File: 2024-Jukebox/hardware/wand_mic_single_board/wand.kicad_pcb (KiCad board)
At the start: 4 copper layers, 17.5 x 39 mm, 50 parts, among them J1 USB_C_Receptacle_USB2.0, J10 Conn_01x03, J4 Conn_01x02, J6 Conn_01x01, J9 Conn_01x02, Q1 MUN5214DW1T1G, Q3 CJ3139K, U1 CP2104, U2 ESP32-PICO-D4, U3 ICM-20948, U4 TP4065-4.2V, U5 TLV76718DRVx, U6 LY68L6400SLIT, U7 PCA9306, U9 TLV76733DRVx

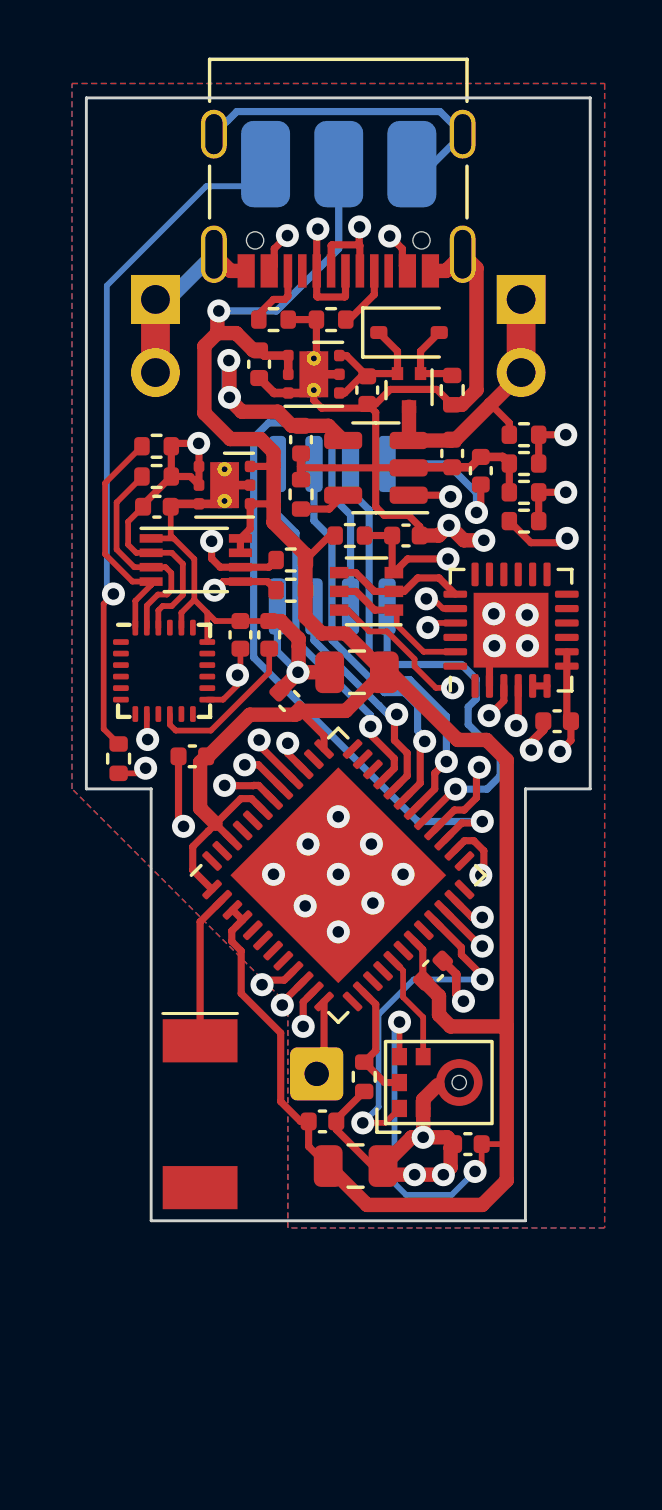
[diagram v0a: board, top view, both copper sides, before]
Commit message: Added some extra silkscreen indicators
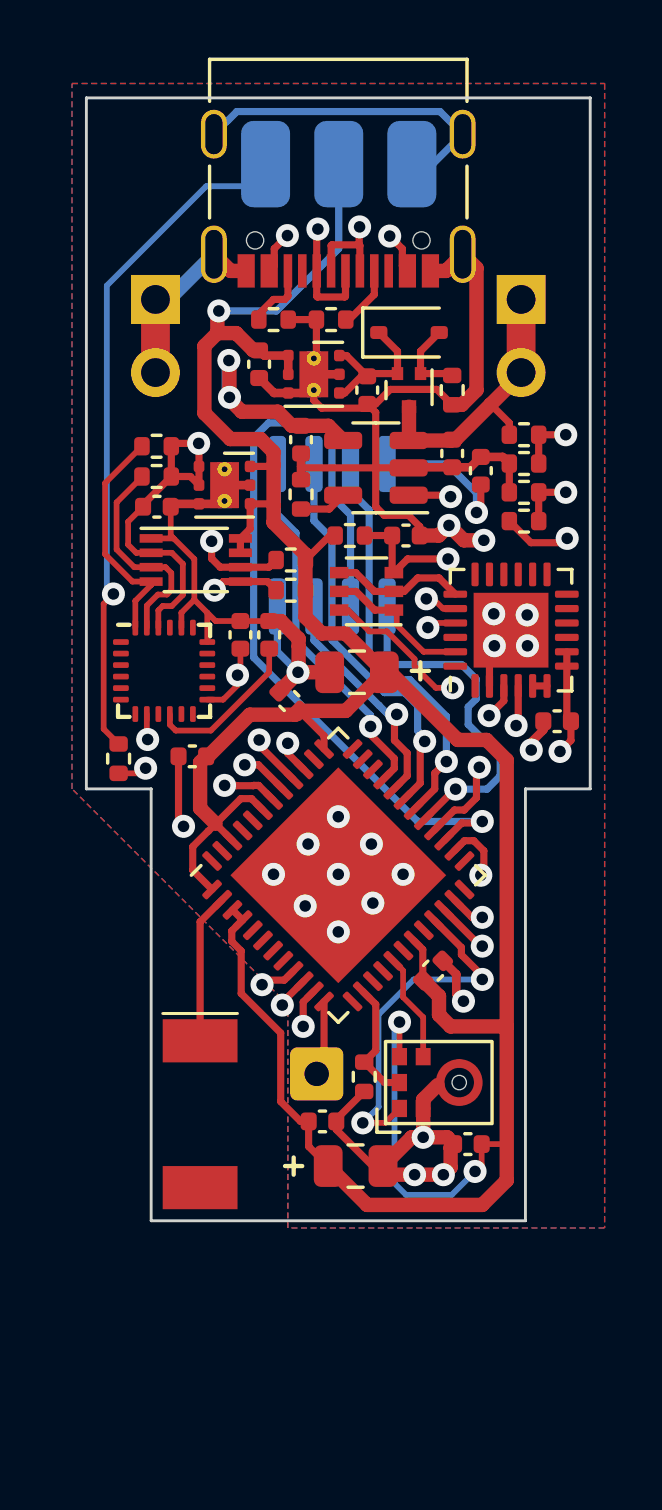
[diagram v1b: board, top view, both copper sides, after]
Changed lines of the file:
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@@
   (gr_line (start 12.95 32.8) (end 12.95 34.2)
     (stroke (width 0.15) (type default)) (layer "B.SilkS"))
+  (gr_line (start 7.2 36.8) (end 7.2 37.4)
+    (stroke (width 0.15) (type default)) (layer "F.SilkS"))
+  (gr_line (start 11.3 19.9) (end 11.9 19.9)
+    (stroke (width 0.15) (type default)) (layer "F.SilkS"))
+  (gr_line (start 11.6 19.6) (end 11.6 20.2)
+    (stroke (width 0.15) (type default)) (layer "F.SilkS"))
+  (gr_line (start 6.9 37.1) (end 7.5 37.1)
+    (stroke (width 0.15) (type default)) (layer "F.SilkS"))
   (gr_line (start 17.5 0) (end 17.5 24)
     (stroke (width 0.1) (type default)) (layer "Edge.Cuts"))
@@
   (segment (start 8.255025 31.384062) (end 8.255025 33.644975) (width 0.25) (layer "F.Cu") (net 92))
   (segment (start 8.255025 33.644975) (end 8 33.9) (width 0.25) (layer "F.Cu") (net 92))
+  (zone (net 0) (net_name "") (layers "F.Cu" "In1.Cu" "In2.Cu" "B.Cu") (hatch edge 0.5)
+    (connect_pads (clearance 0))
+    (min_thickness 0.25) (filled_areas_thickness no)
+    (keepout (tracks not_allowed) (vias not_allowed) (pads not_allowed) (copperpour not_allowed) (footprints allowed))
+    (fill (thermal_gap 0.5) (thermal_bridge_width 0.5))
+    (polygon
+      (pts
+        (xy 1.6 18.8)
+        (xy 1.6 21)
+        (xy 3.8 21)
+        (xy 3.8 18.8)
+      )
+    )
+  )
   (zone (net 6) (net_name "GND") (layers "F.Cu" "In1.Cu" "In2.Cu" "B.Cu") (hatch edge 0.5)
     (connect_pads (clearance 0.508))

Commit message: Updated wand PCBs
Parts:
- removed C14, C15: 47u, Capacitor_SMD:C_0805_2012Metric
- added C22: 10u, Capacitor_SMD:C_0402_1005Metric, F.Cu at (3.34, 30.4)
- added C23: 10u, Capacitor_SMD:C_0402_1005Metric, F.Cu at (3.35, 41.5)
- added C24: 10u, Capacitor_SMD:C_0402_1005Metric, F.Cu at (14.2, 32.9)
- added C25: 10u, Capacitor_SMD:C_0402_1005Metric, F.Cu at (12.5, 42.2)
- C9: footprint Capacitor_SMD:C_0402_1005Metric -> Capacitor_SMD:C_0603_1608Metric
- moved J10 28.3 mm to (13.5, 29.7), turned to 0 degrees
- moved C16 22.5 mm to (11.8, 43.0), turned to -45 degrees
- moved C5 20.2 mm to (7.70, 32.2), turned to 45 degrees
- moved C11 17.3 mm to (13.2, 24.9), turned to 0 degrees
- moved U9 14.6 mm to (13.5, 23.1), turned to 90 degrees
- moved C3 14.2 mm to (11.9, 8.15), turned to 90 degrees
- moved R11 14.1 mm to (11.4, 32.6), turned to -135 degrees
- moved J6 13.1 mm to (13.8, 45.6)
- moved C10 12.0 mm to (15.1, 20.9), turned to 180 degrees
- moved D1 11.7 mm to (14.3, 19.4), turned to 180 degrees
- moved R18 10.8 mm to (13.1, 20.9), turned to 180 degrees
- moved U2 10.8 mm to (8.75, 37.8), turned to 135 degrees
- moved AE1 10.2 mm to (5.95, 45.4), turned to 180 degrees
- moved U5 10.1 mm to (10.8, 21.6), turned to -90 degrees
- moved U1 9.99 mm to (8.75, 10.5), turned to 180 degrees
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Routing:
- net GND: track 94.0 -> 146.8 mm
- net VBUS: track 49.5 -> 23.9 mm, vias 6 -> 0
- net RXD: track 11.7 -> 33.3 mm
- net GPIO10: track 12.4 -> 33.8 mm
- net TXD: track 14.3 -> 35.0 mm
- net Net-(J10-Pin_1): track 23.6 -> 4.51 mm
- net GPIO2: track 19.7 -> 1.56 mm, vias 2 -> 0
- net GPIO25: track 4.33 -> 21.6 mm, vias 0 -> 2
- net GPIO0: track 15.5 -> 32.6 mm
- net GPIO7: track 8.15 -> 23.5 mm
- net IMU_SCL: track 12.3 -> 27.6 mm
- net RESET: track 24.0 -> 39.2 mm
- net GPIO9: track 17.5 -> 32.2 mm
- net Net-(U1-D+): track 27.1 -> 12.6 mm
- net IMU_SDA: track 12.4 -> 26.3 mm
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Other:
- board size 17.5 x 39 mm -> 17.5 x 47 mm
- board text added: "SRAM"

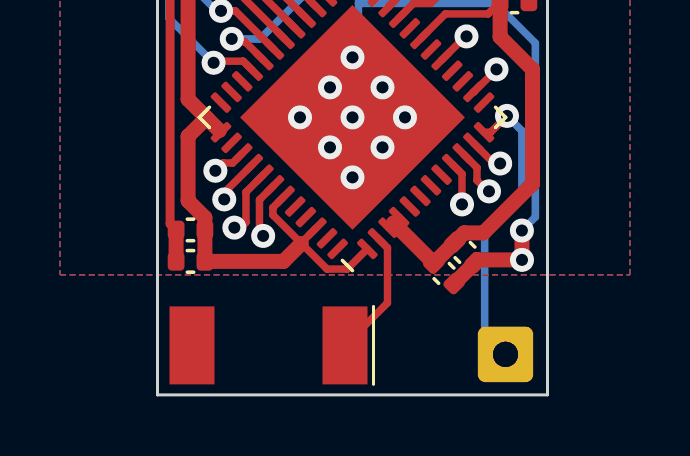
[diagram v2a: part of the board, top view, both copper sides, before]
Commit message: Added 3D models
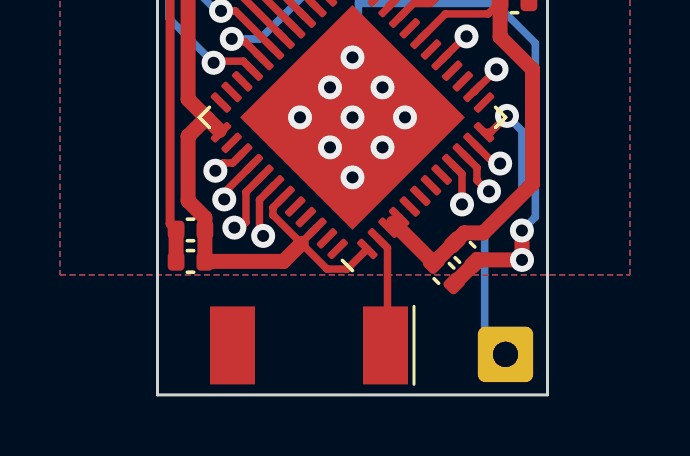
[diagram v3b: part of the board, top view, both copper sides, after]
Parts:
- moved AE1 1.35 mm to (7.30, 45.4)
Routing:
- net Net-(AE1-FEED): track 4.29 -> 3.73 mm
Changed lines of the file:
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@@
   (net 92 "Net-(J6-Pin_1)")
   (footprint "AlexCustom:NN01-102" (layer "F.Cu")
-    (at 5.95 45.35 180)
+    (at 7.3 45.35 180)
     (property "Sheetfile" "wand.kicad_sch")
     (property "Sheetname" "")
@@
     (pad "2" smd rect (at 2.55 0 180) (size 1.5 2.6) (layers "F.Cu" "F.Paste" "F.Mask")
       (net 90 "unconnected-(AE1-PCB_Trace-Pad2)") (pinfunction "PCB_Trace") (pintype "passive") (thermal_bridge_angle 45))
+    (model "${KIPRJMOD}/cad/NN01-102--3DModel-STEP-56544.STEP"
+      (offset (xyz 0 0 0))
+      (scale (xyz 1 1 1))
+      (rotate (xyz -90 0 0))
+    )
   )
   (footprint "Resistor_SMD:R_0402_1005Metric" (layer "F.Cu")
@@
     (pad "2" thru_hole oval (at 0 -2.54 180) (size 1.7 1.7) (drill 1) (layers "*.Cu" "*.Mask")
       (net 6 "GND") (pinfunction "Pin_2") (pintype "passive"))
-    (model "${KICAD6_3DMODEL_DIR}/Connector_PinHeader_2.54mm.3dshapes/PinHeader_1x02_P2.54mm_Vertical.wrl"
-      (offset (xyz 0 0 0))
-      (scale (xyz 1 1 1))
-      (rotate (xyz 0 0 0))
-    )
   )
   (footprint "Connector_PinHeader_2.54mm:PinHeader_1x03_P2.54mm_Vertical" (layer "B.Cu")
@@
     (pad "2" thru_hole oval (at 0 -2.54 180) (size 1.7 1.7) (drill 1) (layers "*.Cu" "*.Mask")
       (net 65 "+BATT") (pinfunction "Pin_2") (pintype "passive"))
-    (model "${KICAD6_3DMODEL_DIR}/Connector_PinHeader_2.54mm.3dshapes/PinHeader_1x02_P2.54mm_Vertical.wrl"
-      (offset (xyz 0 0 0))
+    (model "${KIPRJMOD}/cad/wand_battery_switch.step"
+      (offset (xyz -3.75 8 2))
       (scale (xyz 1 1 1))
       (rotate (xyz 0 0 0))
@@
   (segment (start 10.5125 19) (end 11.23 19.7175) (width 0.2) (layer "F.Cu") (net 78))
   (segment (start 9.598528 41.780509) (end 9.916542 42.098523) (width 0.25) (layer "F.Cu") (net 79))
-  (segment (start 9.916542 43.933458) (end 8.5 45.35) (width 0.25) (layer "F.Cu") (net 79))
-  (segment (start 9.916542 42.098523) (end 9.916542 43.933458) (width 0.25) (layer "F.Cu") (net 79))
+  (segment (start 9.916542 45.283458) (end 9.85 45.35) (width 0.25) (layer "F.Cu") (net 79))
+  (segment (start 9.916542 42.098523) (end 9.916542 45.283458) (width 0.25) (layer "F.Cu") (net 79))
   (segment (start 13.264986 40.214986) (end 12.899873 39.849873) (width 0.25) (layer "F.Cu") (net 80))
   (segment (start 14.28 17.73) (end 14.35 17.8) (width 0.25) (layer "F.Cu") (net 80))

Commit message: Updated wand PCB
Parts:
- moved AE1 1.40 mm to (5.90, 45.4)
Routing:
- net Net-(AE1-FEED): track 3.73 -> 4.31 mm
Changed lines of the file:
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@@
   (net 92 "Net-(J6-Pin_1)")
   (footprint "AlexCustom:NN01-102" (layer "F.Cu")
-    (at 7.3 45.35 180)
+    (at 5.9 45.35 180)
     (property "Sheetfile" "wand.kicad_sch")
     (property "Sheetname" "")
@@
         (effects (font (size 1 1) (thickness 0.15)) (justify mirror))
     )
-    (fp_text value "Conn_01x02" (at -20.25 -5.07) (layer "B.Fab")
+    (fp_text value "Conn_01x02" (at 2.37 -1.6 90) (layer "B.Fab")
         (effects (font (size 1 1) (thickness 0.15)) (justify mirror))
     )
@@
         (effects (font (size 1 1) (thickness 0.15)) (justify mirror))
     )
-    (fp_text value "Conn_01x02" (at -20.25 -5.07) (layer "B.Fab")
+    (fp_text value "Conn_01x02" (at -2.17 -1.2 90) (layer "B.Fab")
         (effects (font (size 1 1) (thickness 0.15)) (justify mirror))
     )
@@
       (net 65 "+BATT") (pinfunction "Pin_2") (pintype "passive"))
     (model "${KIPRJMOD}/cad/wand_battery_switch.step"
-      (offset (xyz -3.75 8 2))
+      (offset (xyz -3.75 8 2.5))
       (scale (xyz 1 1 1))
       (rotate (xyz 0 0 0))
@@
   (segment (start 7.397157 25.047157) (end 7.667157 24.777157) (width 0.2) (layer "F.Cu") (net 78))
   (segment (start 10.5125 19) (end 11.23 19.7175) (width 0.2) (layer "F.Cu") (net 78))
+  (segment (start 9.916542 42.098523) (end 9.916542 43.883458) (width 0.25) (layer "F.Cu") (net 79))
   (segment (start 9.598528 41.780509) (end 9.916542 42.098523) (width 0.25) (layer "F.Cu") (net 79))
-  (segment (start 9.916542 45.283458) (end 9.85 45.35) (width 0.25) (layer "F.Cu") (net 79))
-  (segment (start 9.916542 42.098523) (end 9.916542 45.283458) (width 0.25) (layer "F.Cu") (net 79))
+  (segment (start 9.916542 43.883458) (end 8.45 45.35) (width 0.25) (layer "F.Cu") (net 79))
   (segment (start 13.264986 40.214986) (end 12.899873 39.849873) (width 0.25) (layer "F.Cu") (net 80))
   (segment (start 14.28 17.73) (end 14.35 17.8) (width 0.25) (layer "F.Cu") (net 80))

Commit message: Update wand.kicad_pcb
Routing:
- net GND: track 146.8 -> 147.5 mm
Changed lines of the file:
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@@
   (segment (start 9.65 28.042) (end 9.1 28.042) (width 0.25) (layer "F.Cu") (net 6))
   (segment (start 10.6875 11.25) (end 9.5 11.25) (width 0.25) (layer "F.Cu") (net 6))
+  (segment (start 7.4 27) (end 7.4 26.1745) (width 0.25) (layer "F.Cu") (net 6))
   (segment (start 14.375 19.725) (end 14.375 19.7) (width 0.25) (layer "F.Cu") (net 6))
   (segment (start 13.61 20.93) (end 14.57 20.93) (width 0.25) (layer "F.Cu") (net 6))
   (segment (start 14.375 20.735) (end 14.57 20.93) (width 0.25) (layer "F.Cu") (net 6))
+  (segment (start 6.7 27.3) (end 7.1 27.3) (width 0.25) (layer "F.Cu") (net 6))
   (segment (start 14.375 19.7) (end 14.375 20.735) (width 0.25) (layer "F.Cu") (net 6))
   (segment (start 2.669895 31.640105) (end 2.86 31.45) (width 0.3) (layer "F.Cu") (net 6))
@@
   (segment (start 8.2 16.83) (end 8.2 17.37) (width 0.5) (layer "F.Cu") (net 6))
   (segment (start 9.65 28.042) (end 10.918 28.042) (width 0.25) (layer "F.Cu") (net 6))
-  (segment (start 8.0875 26.79) (end 7.247347 26.79) (width 0.25) (layer "F.Cu") (net 6))
+  (segment (start 5.67 28.33) (end 6.7 27.3) (width 0.25) (layer "F.Cu") (net 6))
   (segment (start 6.567157 22.275797) (end 6.238517 21.947157) (width 0.2) (layer "F.Cu") (net 6))
   (segment (start 2.669895 41.299895) (end 2.669895 31.640105) (width 0.3) (layer "F.Cu") (net 6))
   (segment (start 7.1725 16.48) (end 8.18 16.48) (width 0.5) (layer "F.Cu") (net 6))
+  (segment (start 7.4 26.1745) (end 7.8245 25.75) (width 0.25) (layer "F.Cu") (net 6))
   (segment (start 9.4 11.15) (end 9.4 11.05) (width 0.25) (layer "F.Cu") (net 6))
+  (segment (start 7.1 27.3) (end 7.4 27) (width 0.25) (layer "F.Cu") (net 6))
   (segment (start 5.01 6.01) (end 4.43 5.43) (width 0.25) (layer "F.Cu") (net 6))
+  (segment (start 5.67 29.4) (end 5.67 28.33) (width 0.25) (layer "F.Cu") (net 6))
   (segment (start 14.05 6.41) (end 13.07 5.43) (width 0.25) (layer "F.Cu") (net 6))
   (segment (start 7.667157 23.537158) (end 7.667157 23.817157) (width 0.2) (layer "F.Cu") (net 6))
@@
   (segment (start 6.567157 23.047157) (end 6.567157 22.275797) (width 0.2) (layer "F.Cu") (net 6))
   (segment (start 14.15 23.9375) (end 14.15 23.15) (width 0.3) (layer "F.Cu") (net 6))
-  (segment (start 7.247347 26.79) (end 5.67 28.367347) (width 0.25) (layer "F.Cu") (net 6))
   (segment (start 3.67 10.54) (end 3.67 8) (width 1) (layer "F.Cu") (net 6))
   (segment (start 12.928822 42.5) (end 12.839411 42.589411) (width 0.5) (layer "F.Cu") (net 6))
@@
   (segment (start 11.95 6.01) (end 12.49 6.01) (width 0.25) (layer "F.Cu") (net 6))
   (segment (start 14.4 42.5) (end 12.928822 42.5) (width 0.5) (layer "F.Cu") (net 6))
-  (segment (start 5.67 28.367347) (end 5.67 29.4) (width 0.25) (layer "F.Cu") (net 6))
   (segment (start 11.95 7.67) (end 11.95 6.01) (width 0.25) (layer "F.Cu") (net 6))
   (segment (start 9.3 11.05) (end 8.75 10.5) (width 0.25) (layer "F.Cu") (net 6))

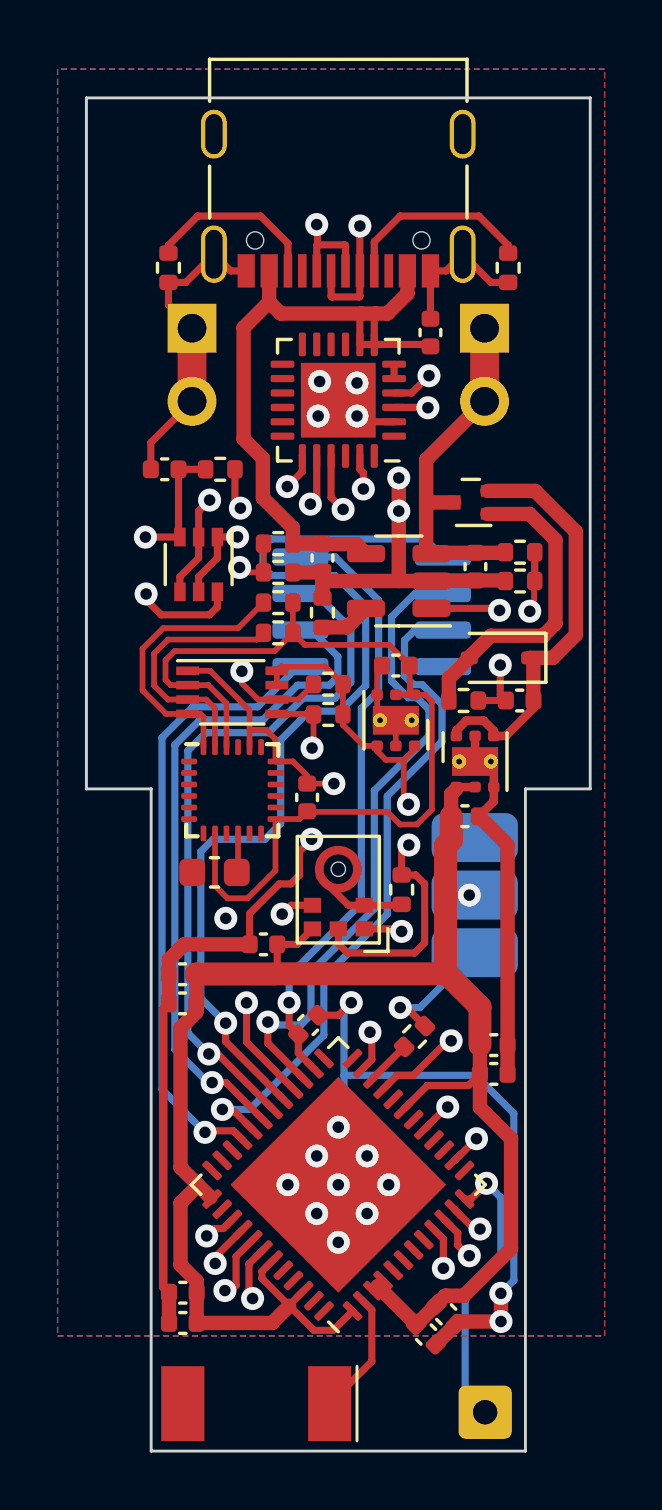
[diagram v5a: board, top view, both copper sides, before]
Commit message: Fixed wiring issue
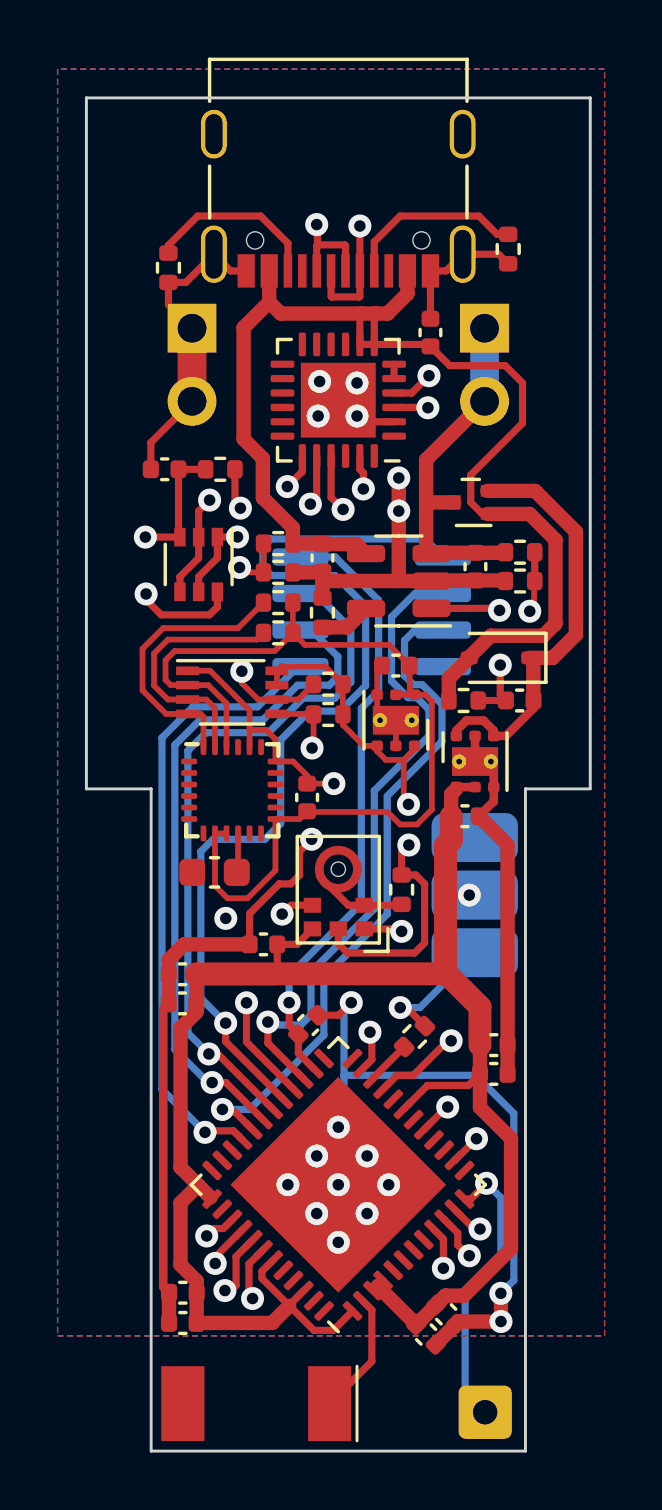
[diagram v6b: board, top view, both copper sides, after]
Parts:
- moved R2 0.65 mm to (14.7, 5.25)
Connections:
- D1 pad 2: Net-(D1-A) -> VBUS
- Q3 pad 1: Net-(D1-A) -> VBUS
- R18 pad 2: Net-(D1-A) -> VBUS
- U3 pad 9: unconnected-(U3-SDO/AD0-Pad9) -> +1V8
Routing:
- net VBUS: track 23.9 -> 44.2 mm
- net Net-(D1-A): track 10.9 -> 0.00 mm

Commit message: Update wand.kicad_pcb
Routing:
- net GND: track 147.2 -> 150.3 mm
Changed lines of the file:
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@@
   (segment (start 10.85 14.35) (end 10.85 13.2) (width 0.5) (layer "F.Cu") (net 5))
   (segment (start 5.667157 22.547157) (end 5.667157 21.947157) (width 0.2) (layer "F.Cu") (net 5))
+  (segment (start 3.675 26.9) (end 2.65 25.875) (width 0.25) (layer "F.Cu") (net 5))
   (segment (start 12.49 6.01) (end 13.07 5.43) (width 0.25) (layer "F.Cu") (net 5))
   (segment (start 7.177156 23.047157) (end 7.667157 23.537158) (width 0.2) (layer "F.Cu") (net 5))
@@
   (segment (start 9.1 28.042) (end 8.0875 27.0295) (width 0.25) (layer "F.Cu") (net 5))
   (segment (start 5.55 6.01) (end 5.01 6.01) (width 0.25) (layer "F.Cu") (net 5))
+  (segment (start 2.65 25.875) (end 2.65 24.2) (width 0.25) (layer "F.Cu") (net 5))
   (segment (start 6.238517 21.947157) (end 5.667157 21.947157) (width 0.2) (layer "F.Cu") (net 5))
   (segment (start 2.24 11.97) (end 3.67 10.54) (width 0.25) (layer "F.Cu") (net 5))
